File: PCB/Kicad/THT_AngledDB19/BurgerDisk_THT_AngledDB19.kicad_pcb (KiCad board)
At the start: 2 copper layers, 93.7 x 73.4 mm, 18 parts, among them J1 Daisy port in, J2 MicroSD module, J3 UART, J4 Daisy port out, U1 PC817

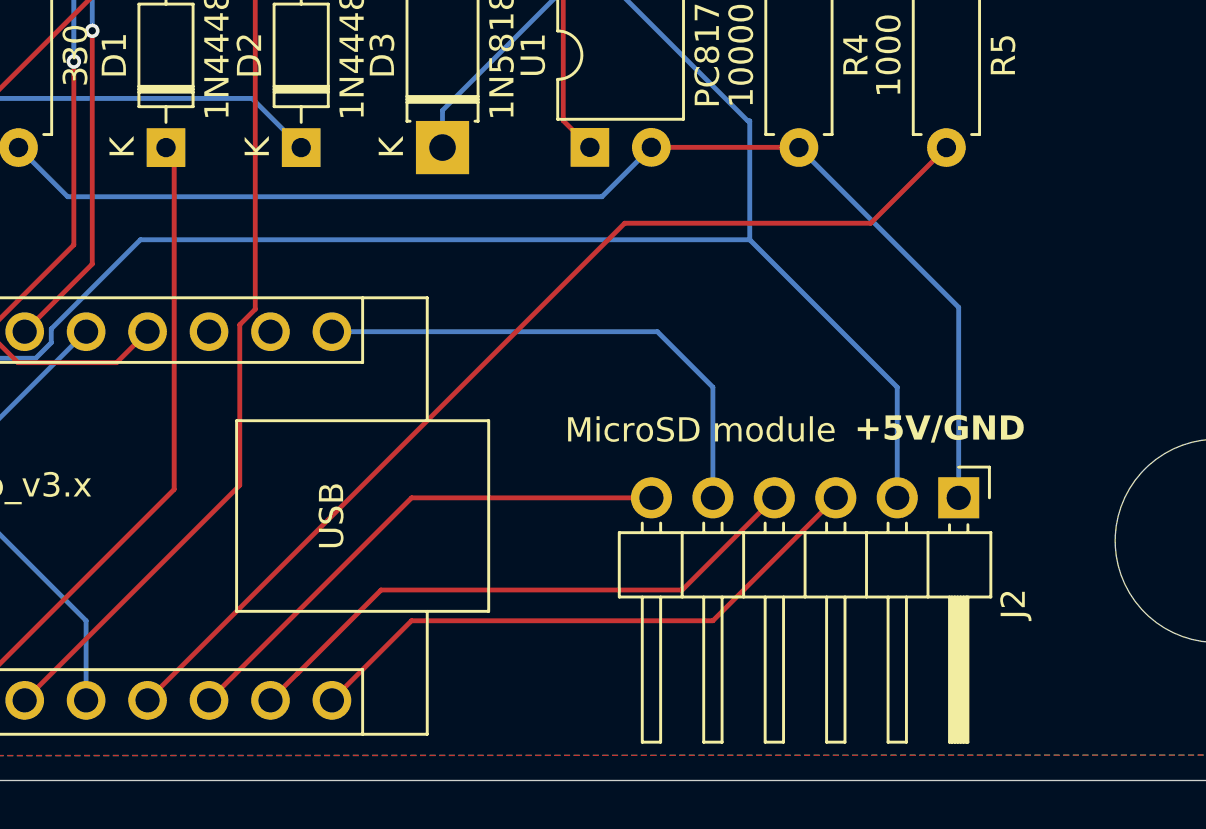
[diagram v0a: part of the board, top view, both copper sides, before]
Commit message: Add 8-pin header for full size SD module
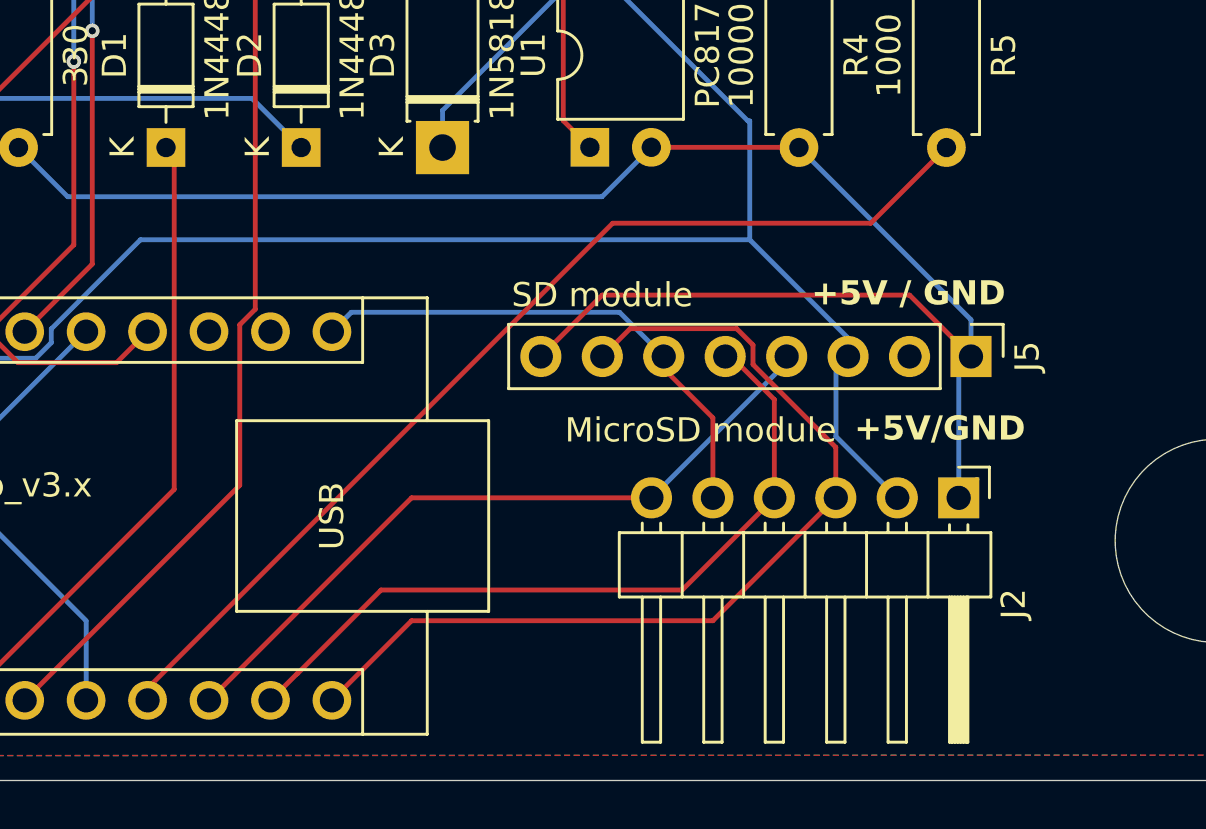
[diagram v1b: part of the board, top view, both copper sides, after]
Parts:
- added J5: SD module, Connector_PinHeader_2.54mm:PinHeader_1x08_P2.54mm_Vertical, F.Cu at (146.8, 93.7)
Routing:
- net GND: track 182.5 -> 203.9 mm
- net MISO: track 24.3 -> 39.0 mm
- net CS: track 21.8 -> 29.9 mm
- net MOSI: track 24.3 -> 30.9 mm
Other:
- board text added: "+5V / GND"

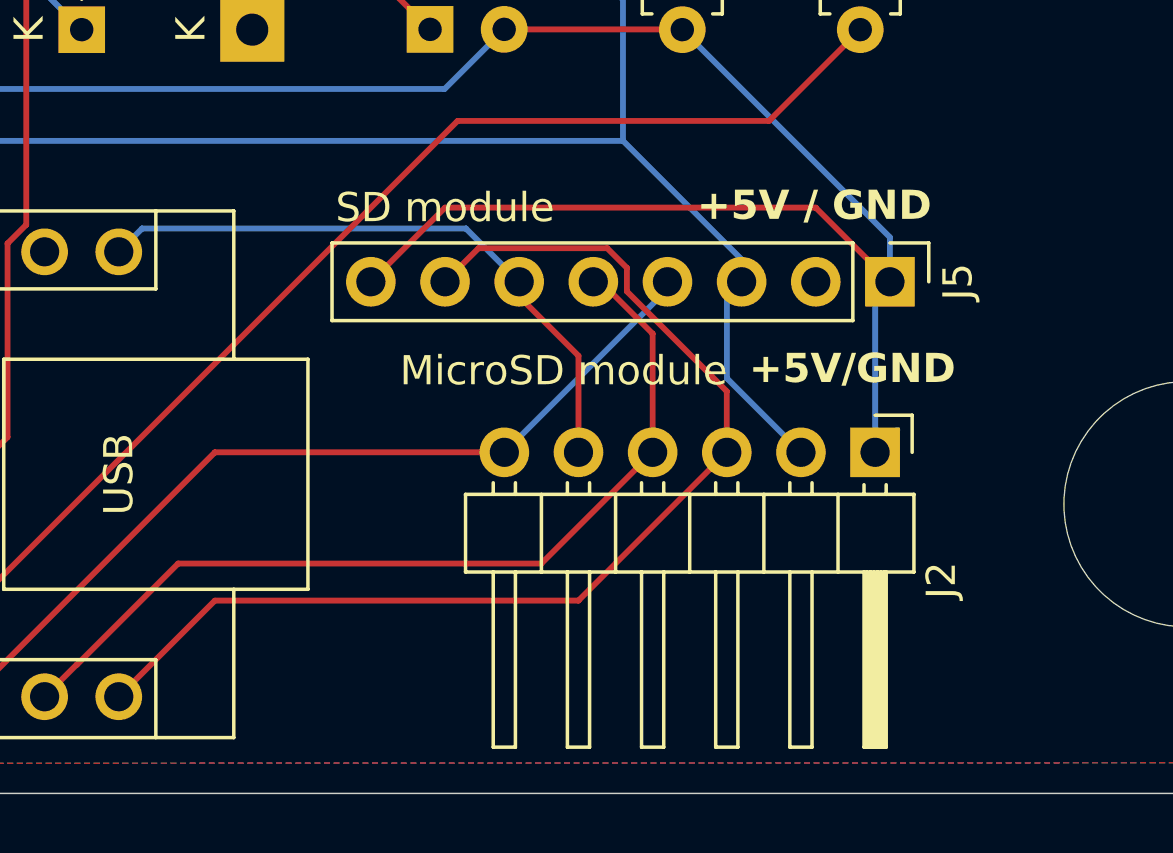
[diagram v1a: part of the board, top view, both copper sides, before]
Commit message: Vertical footprints
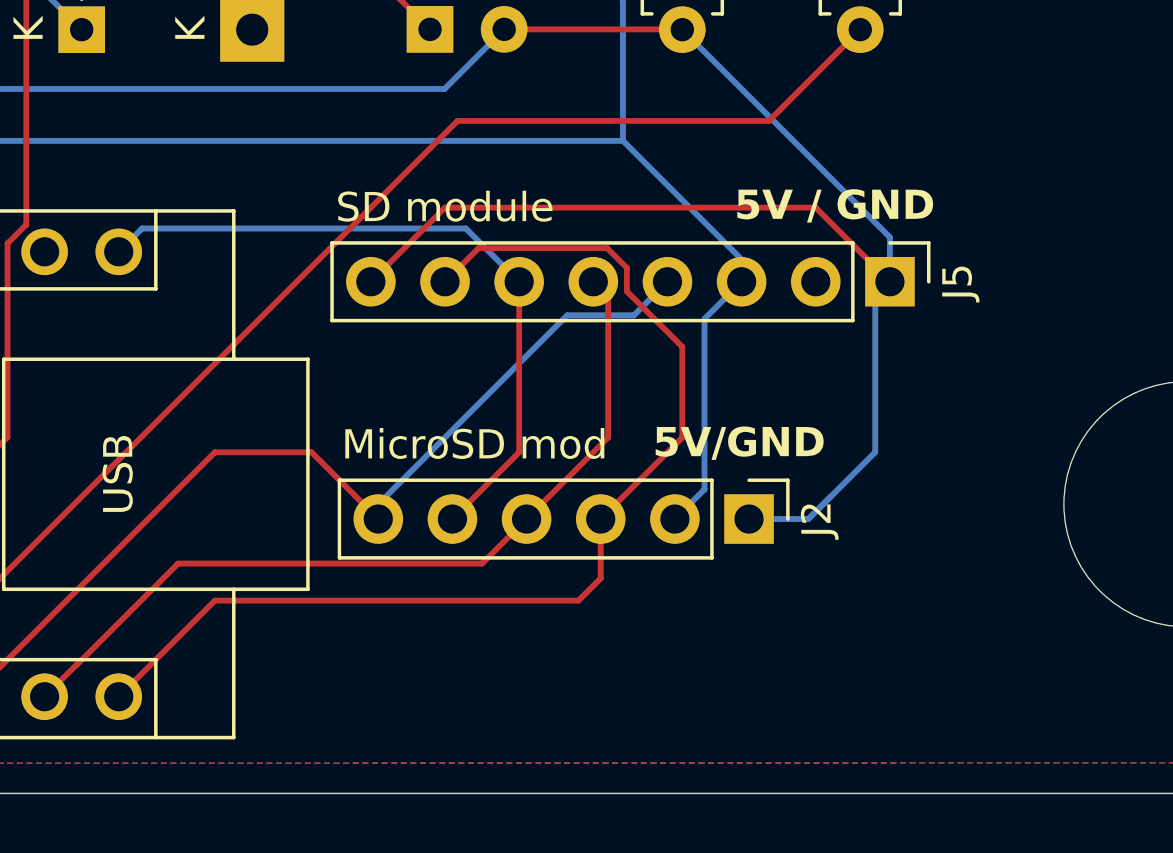
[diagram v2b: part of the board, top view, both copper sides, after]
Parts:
- J2: value MicroSD module -> MicroSD mod; footprint Connector_PinHeader_2.54mm:PinHeader_1x06_P2.54mm_Horizontal -> Connector_PinHeader_2.54mm:PinHeader_1x06_P2.54mm_Vertical
- moved J2 4.89 mm to (142.0, 101.9)
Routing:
- net GND: track 203.9 -> 209.2 mm
- net MOSI: track 30.9 -> 28.4 mm
- net SCK: track 21.5 -> 23.9 mm
- net CS: track 29.9 -> 32.0 mm
- net 5V_burgerDisk: track 86.0 -> 88.0 mm
- net MISO: track 39.0 -> 37.8 mm
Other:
- board text added: "5V / GND"
- board text added: "5V/GND"
- board text removed: "+5V / GND"
- board text removed: "+5V/GND"

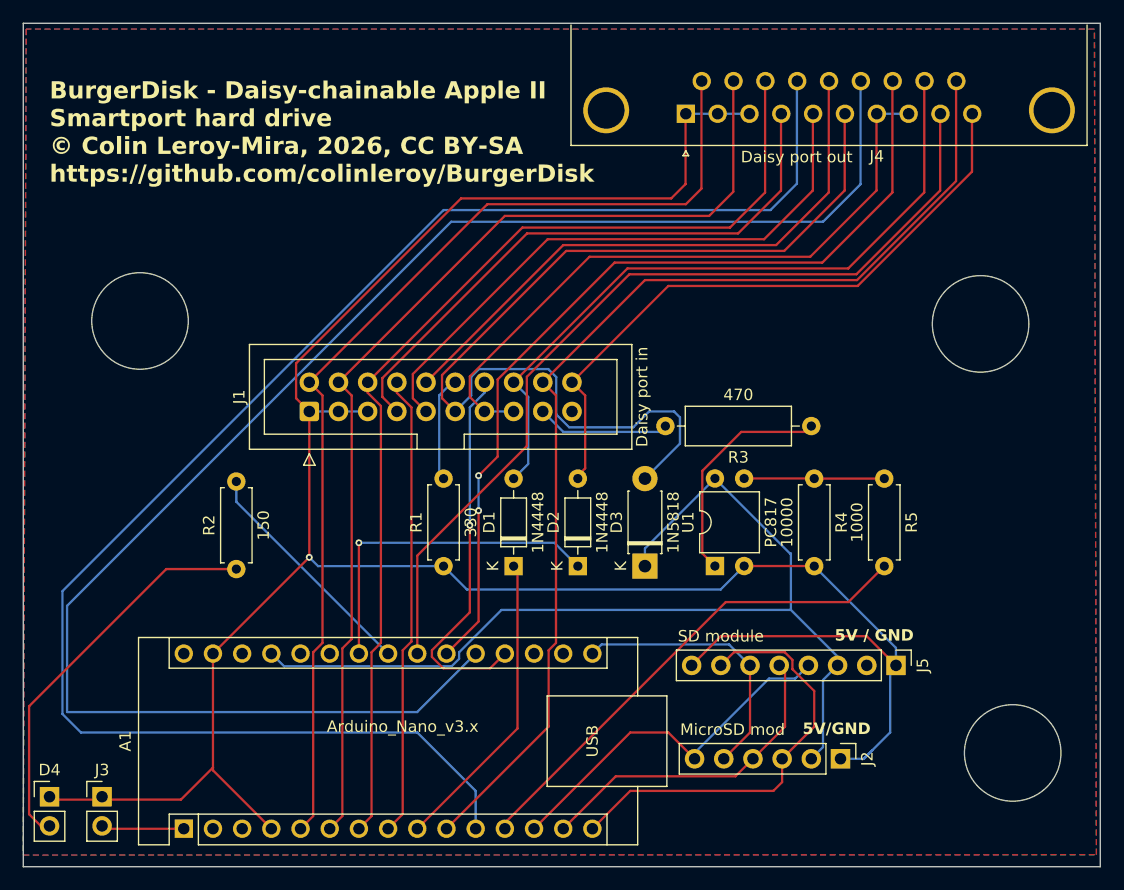
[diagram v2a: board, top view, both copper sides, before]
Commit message: Revert full-size SD connector and module.
They don't have level shifter.
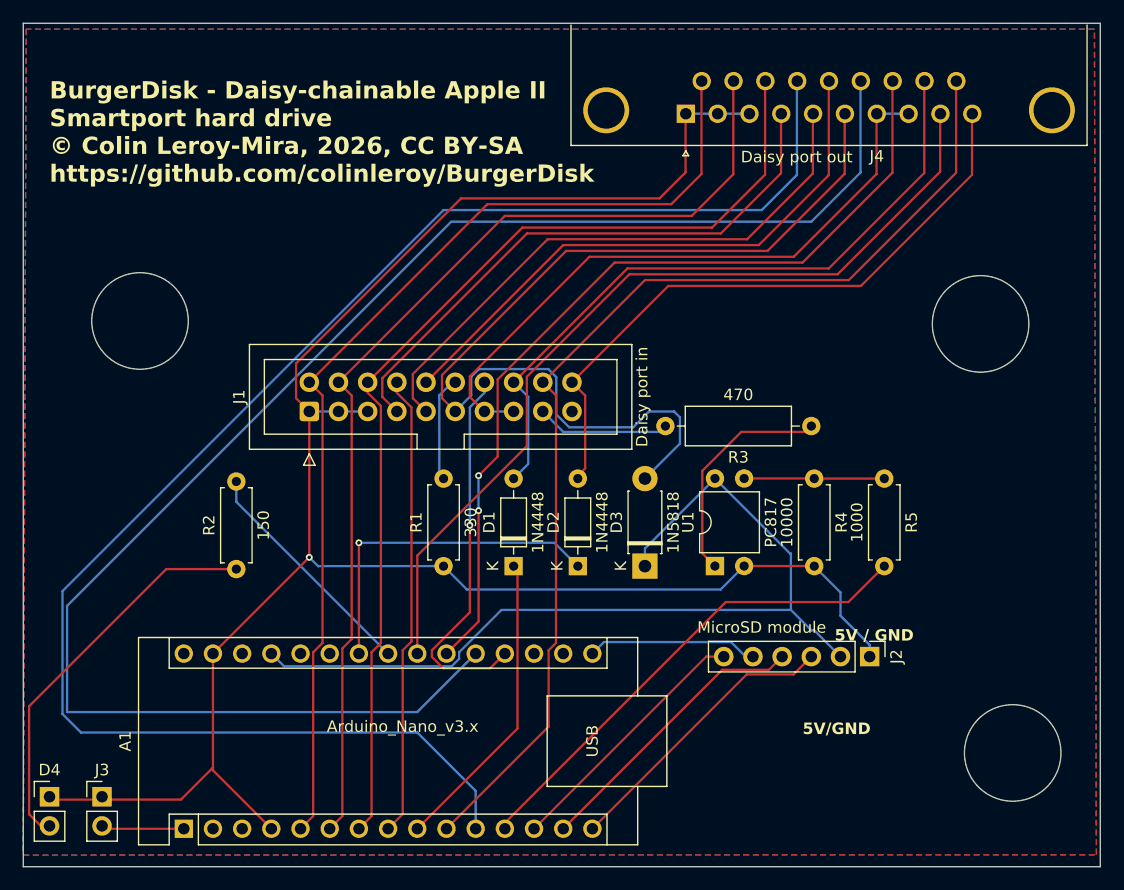
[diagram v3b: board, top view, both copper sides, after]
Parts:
- removed J5: SD module, Connector_PinHeader_2.54mm:PinHeader_1x08_P2.54mm_Vertical
- J2: value MicroSD mod -> MicroSD module
- moved J2 9.25 mm to (144.5, 93.0)
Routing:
- net GND: track 209.2 -> 174.6 mm
- net MISO: track 37.8 -> 25.3 mm
- net 5V_burgerDisk: track 88.0 -> 78.4 mm
- net CS: track 32.0 -> 22.7 mm
- net SCK: track 23.9 -> 15.8 mm
- net MOSI: track 28.4 -> 25.3 mm
- net DRV1_out: track 76.5 -> 75.5 mm
- net RDDATA_out: track 61.7 -> 60.7 mm
- net DRV2_out: track 77.4 -> 76.5 mm
- net PH2: track 91.2 -> 90.3 mm
- net PH1: track 91.0 -> 90.1 mm
- net WREQ: track 51.6 -> 50.7 mm
- net EN3.5: track 51.6 -> 50.7 mm
- net -12V: track 51.8 -> 51.0 mm
- net 5V_apple2: track 85.4 -> 84.6 mm
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
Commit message: Align connectors
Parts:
- moved J2 14.7 mm to (144.5, 107.7)
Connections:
- J4 pad 0: (no net) -> GND
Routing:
- net GND: track 174.6 -> 233.1 mm
- net 5V_burgerDisk: track 78.4 -> 93.1 mm
- net SCK: track 15.8 -> 29.3 mm
- net CS: track 22.7 -> 17.9 mm
- net MISO: track 25.3 -> 21.4 mm
- net MOSI: track 25.3 -> 22.5 mm
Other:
- board text removed: "5V / GND"
